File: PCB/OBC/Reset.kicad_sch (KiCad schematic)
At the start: 25 parts, among them U2 STM32F405RGTx

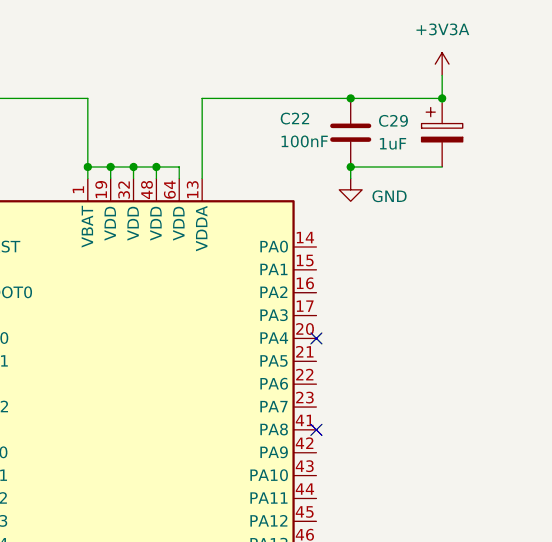
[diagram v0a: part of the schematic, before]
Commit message: Add: flash memory and mux at libraries
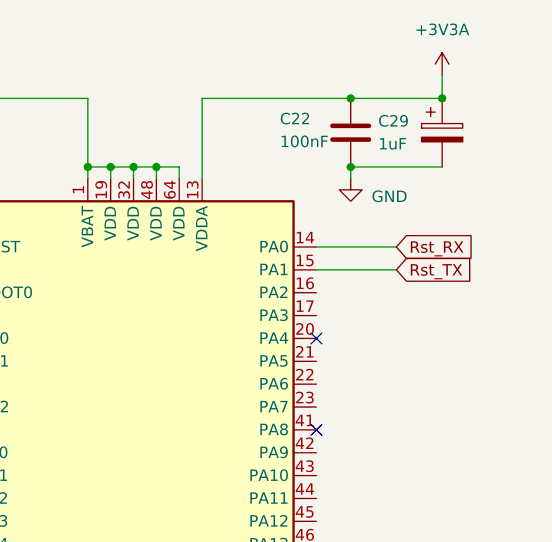
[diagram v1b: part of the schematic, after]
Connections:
- net Rst_RX: now reaches U2.14 (PA0)
- net Rst_TX: now reaches U2.15 (PA1)
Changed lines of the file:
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@@
+	(wire
+		(pts
+			(xy 146.05 41.91) (xy 154.94 41.91)
+		)
+		(stroke
+			(width 0)
+			(type default)
+		)
+	)
 	(wire
 		(pts
@@
 		(pts
 			(xy 52.07 34.29) (xy 52.07 33.02)
+		)
+		(stroke
+			(width 0)
+			(type default)
+		)
+	)
+	(wire
+		(pts
+			(xy 146.05 44.45) (xy 154.94 44.45)
 		)
 		(stroke
@@
 			)
 			(justify right bottom)
+		)
+	)
+	(global_label "Rst_TX"
+		(shape input)
+		(at 154.94 44.45 0)
+		(fields_autoplaced yes)
+		(effects
+			(font
+				(size 1.27 1.27)
+			)
+			(justify left)
+		)
+		(property "Intersheetrefs" "${INTERSHEET_REFS}"
+			(at 164.0937 44.45 0)
+			(effects
+				(font
+					(size 1.27 1.27)
+				)
+				(justify left)
+				(hide yes)
+			)
 		)
 	)
@@
 				(hide yes)
 			)
+		)
+	)
+	(global_label "Rst_RX"
+		(shape input)
+		(at 154.94 41.91 0)
+		(fields_autoplaced yes)
+		(effects
+			(font
+				(size 1.27 1.27)
+			)
+			(justify left)
+		)
+		(property "Intersheetrefs" "${INTERSHEET_REFS}"
+			(at 164.3961 41.91 0)
+			(effects
+				(font
+					(size 1.27 1.27)
+				)
+				(justify left)
+				(hide yes)
+			)

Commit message: Watchdog
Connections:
- net set_0: now reaches U2.44 (PA11)
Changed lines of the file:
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@@
+	(wire
+		(pts
+			(xy 146.05 69.85) (xy 152.4 69.85)
+		)
+		(stroke
+			(width 0)
+			(type default)
+		)
+	)
 	(wire
 		(pts
@@
 			(effects
 				(font
+					(size 1.27 1.27)
+				)
+				(justify left)
+				(hide yes)
+			)
+		)
+	)
+	(global_label "set_0"
+		(shape input)
+		(at 152.4 69.85 0)
+		(fields_autoplaced yes)
+		(effects
+			(font
+				(size 1.27 1.27)
+			)
+			(justify left)
+		)
+		(property "Intersheetrefs" "${INTERSHEET_REFS}"
+			(at 160.4047 69.85 0)
+			(effects
+				(font

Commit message: minors changes
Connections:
- net Rst_RX: now also U2.37 (PC6)
- net Rst_TX: now also U2.38 (PC7)
- net set_0: now also U2.23 (PA7); no longer U2.44 (PA11)
- net set_1: now reaches U2.24 (PC4)
- net set_2: now reaches U2.25 (PC5)
- net EN_PY1: now reaches U2.52 (PC11)
- net EN_ADCS: now reaches U2.54 (PD2)
- net EN_COMS: now reaches U2.56 (PB4)
- net EN_PY2: now reaches U2.58 (PB6)
- no-connect marks 7 -> 38

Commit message: cambiode OCP
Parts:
- removed C20, C21: 2.2uF, Capacitor_SMD:C_0805_2012Metric_Pad1.18x1.45mm_HandSolder, symbol Device:C
- removed C22, C23, C25, C27, C32: 100nF, Capacitor_SMD:C_0603_1608Metric_Pad1.08x0.95mm_HandSolder, symbol Device:C
- removed C24, C26: 100nF, Capacitor_SMD:C_0805_2012Metric_Pad1.18x1.45mm_HandSolder, symbol Device:C
- removed C28: 4.7u, Capacitor_SMD:C_0805_2012Metric_Pad1.18x1.45mm_HandSolder, symbol Device:C_Polarized
- removed C29: 1uF, Capacitor_SMD:C_0805_2012Metric_Pad1.18x1.45mm_HandSolder, symbol Device:C_Polarized
- removed C5, C6: 15pF, Capacitor_SMD:C_0603_1608Metric_Pad1.08x0.95mm_HandSolder, symbol Device:C
- removed D8: LED, LED_SMD:LED_0805_2012Metric_Pad1.15x1.40mm_HandSolder, symbol Device:LED
- removed R14: 10k, Resistor_SMD:R_0805_2012Metric_Pad1.20x1.40mm_HandSolder, symbol Device:R
- removed R19, R20: 330, Resistor_SMD:R_0805_2012Metric_Pad1.20x1.40mm_HandSolder, symbol Device:R
- removed SwBoot1: SW_Nidec_CAS-120A1, Button_Switch_SMD:Nidec_Copal_CAS-120A, symbol Switch:SW_Nidec_CAS-120A1
- removed SwReset1: SW_Push, Button_Switch_SMD:SW_Push_SPST_NO_Alps_SKRK, symbol Switch:SW_Push
- removed U2: STM32F405RGTx, Package_QFP:LQFP-64_10x10mm_P0.5mm, symbol MCU_ST_STM32F4:STM32F405RGTx
- removed XTAL1: ECS-80-12-30BQ-JES-TR, ESCMHZ:ECS-80-12_ECS, symbol ESC8Mhz:ECS-80-12-30BQ-JES-TR
- added C33, C39: 15pF, Capacitor_SMD:C_0603_1608Metric_Pad1.08x0.95mm_HandSolder, symbol Device:C
- added C34: 4.7u, Capacitor_SMD:C_0805_2012Metric_Pad1.18x1.45mm_HandSolder, symbol Device:C_Polarized
- added C35, C40, C43, C45, C46: 100nF, Capacitor_SMD:C_0603_1608Metric_Pad1.08x0.95mm_HandSolder, symbol Device:C
- added C37, C41: 100nF, Capacitor_SMD:C_0805_2012Metric_Pad1.18x1.45mm_HandSolder, symbol Device:C
- added C42, C44: 2.2uF, Capacitor_SMD:C_0805_2012Metric_Pad1.18x1.45mm_HandSolder, symbol Device:C
- added C47: 1uF, Capacitor_SMD:C_0805_2012Metric_Pad1.18x1.45mm_HandSolder, symbol Device:C_Polarized
- added D6: LED, LED_SMD:LED_0805_2012Metric_Pad1.15x1.40mm_HandSolder, symbol Device:LED
- added R11: 10k, Resistor_SMD:R_0805_2012Metric_Pad1.20x1.40mm_HandSolder, symbol Device:R
- added R12, R13: 330, Resistor_SMD:R_0805_2012Metric_Pad1.20x1.40mm_HandSolder, symbol Device:R
- added SwBoot3: SW_Nidec_CAS-120A1, Button_Switch_SMD:Nidec_Copal_CAS-120A, symbol Switch:SW_Nidec_CAS-120A1
- added SwReset3: SW_Push, Button_Switch_SMD:SW_Push_SPST_NO_Alps_SKRK, symbol Switch:SW_Push
- added U5: STM32F405RGTx, Package_QFP:LQFP-64_10x10mm_P0.5mm, symbol MCU_ST_STM32F4:STM32F405RGTx
- added XTAL3: ECS-80-12-30BQ-JES-TR, ECS-80-12-30BQ-JES-TR:ECS-80-12_ECS, symbol ESC8Mhz:ECS-80-12-30BQ-JES-TR
- renumbered C7 to C36, C8 to C38, FB1 to FB3
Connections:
- net +3V3: now also C34.1, C35.1, C37.1, C40.1, C41.1, C43.1, SwBoot3.1 (C), U5.1 (VBAT), U5.19 (VDD), U5.32 (VDD), U5.48 (VDD), U5.64 (VDD)
- net +3V3A: now also C46.1, C47.1, U5.13 (VDDA)
- net BOOT0: now also R11.2, U5.60 (BOOT0)
- net EN_ADCS: now also U5.54 (PD2)
- net EN_COMS: now also U5.56 (PB4)
- net EN_PY1: now also U5.52 (PC11)
- net EN_PY2: now also U5.58 (PB6)
- net GND: now also C33.2, C34.2, C35.2, C37.2, C39.2, C40.2, C41.2, C42.2, C43.2, C44.2, C45.2, C46.2, C47.2, D6.1 (K), SwBoot3.3 (A), SwReset3.1, U5.12 (VSSA), U5.18 (VSS), U5.63 (VSS), XTAL3.2, XTAL3.4
- net HSE_IN: now also C33.1, U5.5 (PH0), XTAL3.1
- net HSE_OUT: now also C39.1, U5.6 (PH1), XTAL3.3
- net LGreen: now also R13.1
- net LRed: now also R12.1
- net Rst_RX: now also U5.14 (PA0), U5.37 (PC6)
- net Rst_TX: now also U5.15 (PA1), U5.38 (PC7)
- net SWD_NRST: now also C45.1, SwReset3.2, U5.7 (NRST)
- net set_0: now also U5.23 (PA7)
- net set_1: now also U5.24 (PC4)
- net set_2: now also U5.25 (PC5)
- net at D7.2 (A): now also R13.2
- new net: D6.2 (A), R12.2
- new net: R11.1, SwBoot3.2 (B)
- new net: C44.1, U5.47 (VCAP_2)
- new net: C42.1, U5.31 (VCAP_1)
